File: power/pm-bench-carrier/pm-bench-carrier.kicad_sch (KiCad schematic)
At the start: 47 parts, among them J1 VIN 40-60V, J2 VOUT 19V, Q1 2N7002

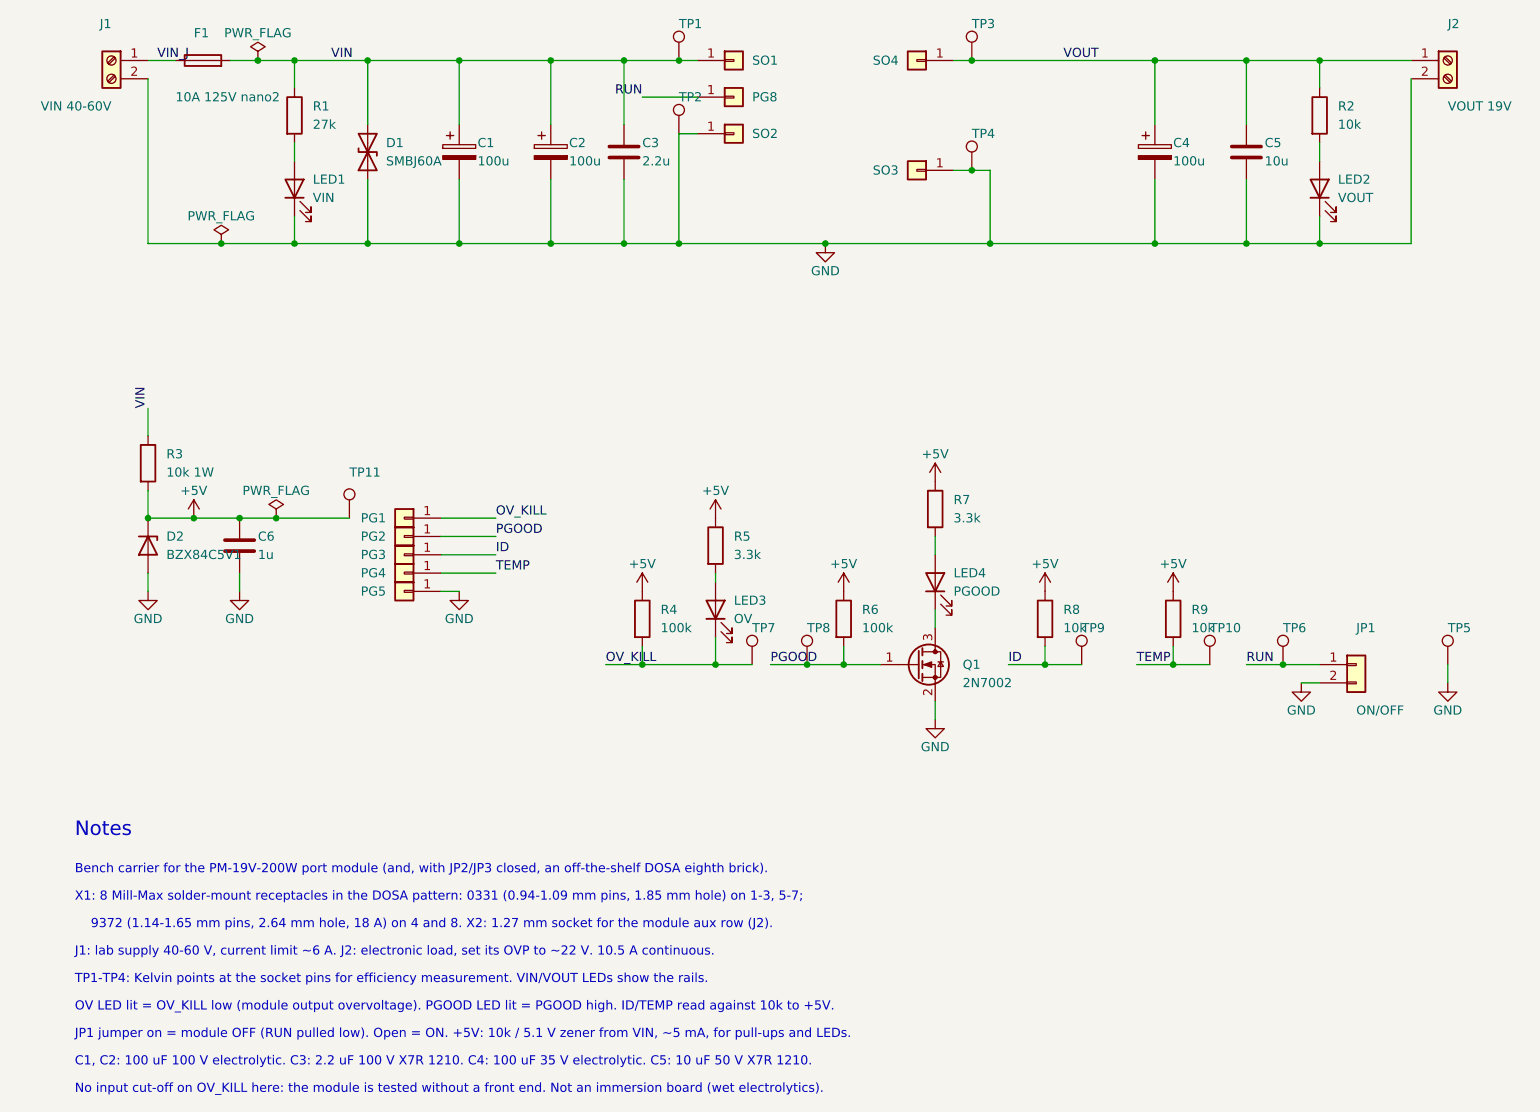
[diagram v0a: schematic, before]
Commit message: Revert "power: screwed PM module mount footprints (M2 into SMT standoffs, pogo aux) on module, plane and bench carrier; RUN moves to aux pad 8; copper not yet rerouted"
This reverts commit abb9f50ba34d0b63e5425fa3cd376420f2890e7d.
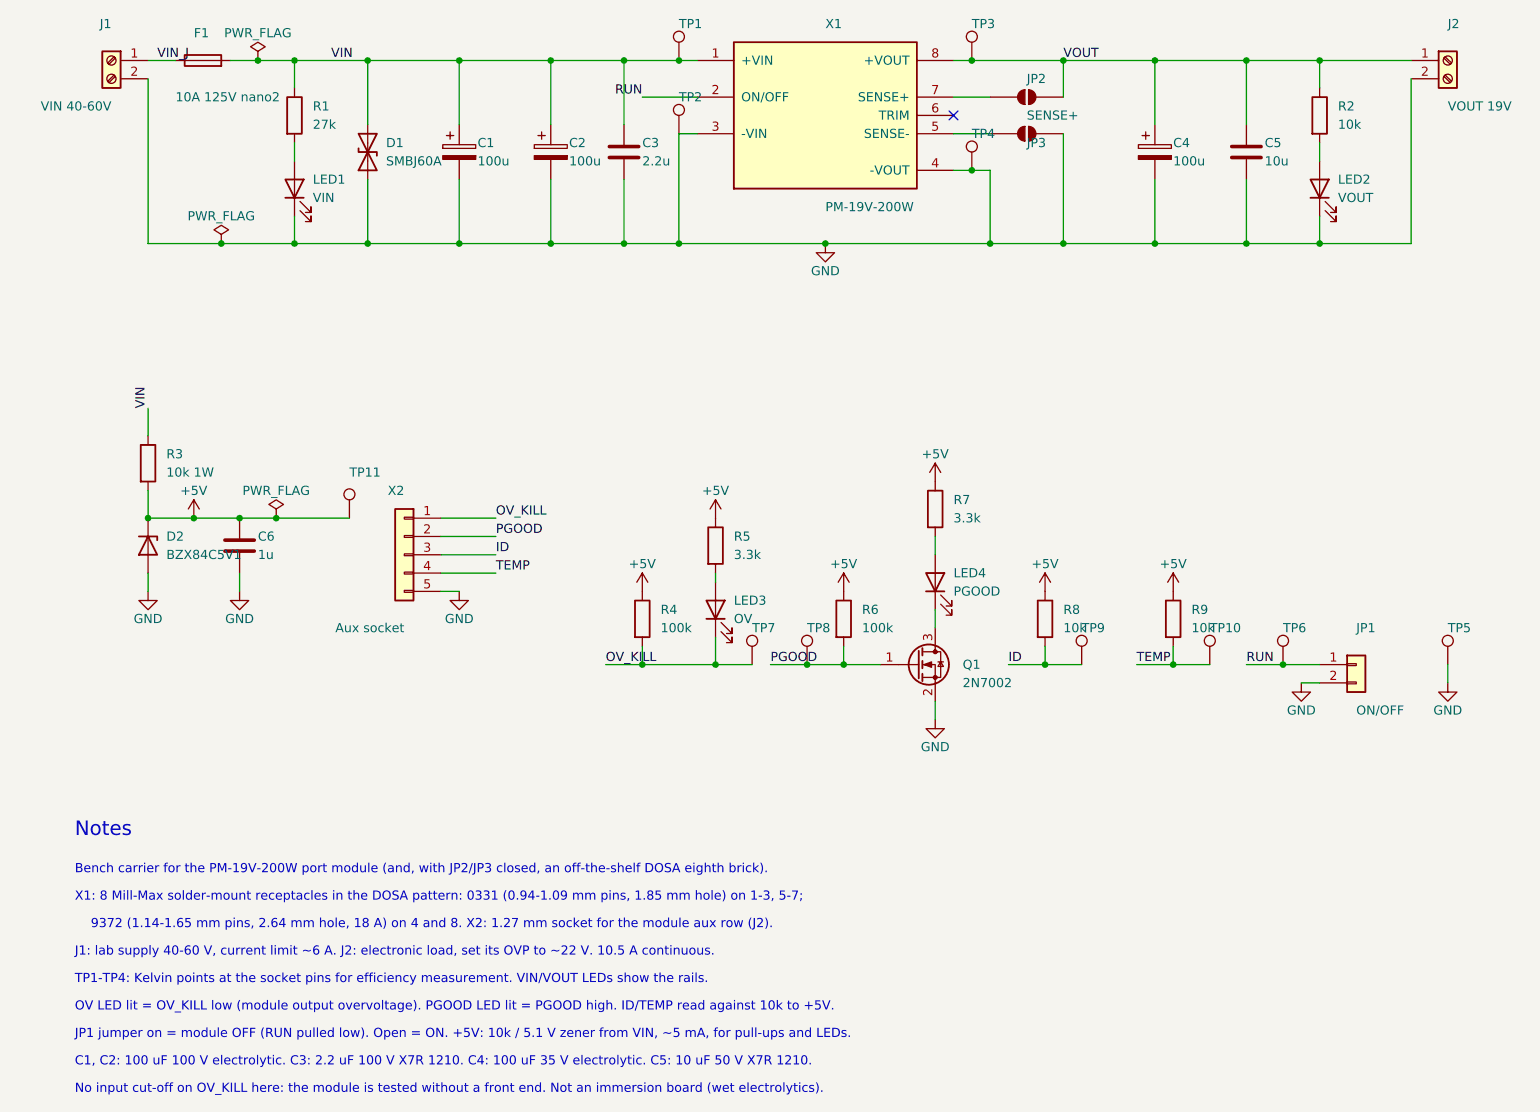
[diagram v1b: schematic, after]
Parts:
- removed PG1, PG2, PG3, PG4, PG5, PG8: pogo, carrier:PM_Pogo_YZ130115073P, symbol Connector_Generic:Conn_01x01
- removed SO1, SO2, SO3, SO4: M2x6 standoff, carrier:PM_Standoff_M2x6_SMTSO, symbol Connector_Generic:Conn_01x01
- added JP2: SENSE+, Jumper:SolderJumper-2_P1.3mm_Open_RoundedPad1.0x1.5mm, symbol Jumper:SolderJumper_2_Open
- added JP3: SENSE-, Jumper:SolderJumper-2_P1.3mm_Open_RoundedPad1.0x1.5mm, symbol Jumper:SolderJumper_2_Open
- added X1: PM-19V-200W, carrier:Brick_Eighth_DOSA_Socket, symbol carrier:PM_Brick_Socket
- added X2: Aux socket, Connector_PinSocket_1.27mm:PinSocket_1x05_P1.27mm_Vertical, symbol Connector_Generic:Conn_01x05
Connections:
- net GND: now also JP3.2 (B), X1.3 (-VIN), X1.4 (-VOUT), X2.5 (Pin_5)
- net ID: now also X2.3 (Pin_3)
- net OV_KILL: now also X2.1 (Pin_1)
- net PGOOD: now also X2.2 (Pin_2)
- net RUN: now also X1.2 (ON/OFF)
- net TEMP: now also X2.4 (Pin_4)
- net VIN: now also X1.1 (+VIN)
- net VOUT: now also JP2.2 (B), X1.8 (+VOUT)
- new net: JP2.1 (A), X1.7 (SENSE+)
- new net: JP3.1 (A), X1.5 (SENSE-)
- no-connect marks 0 -> 1

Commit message: power: screwed PM module mount footprints (M2 into SMT standoffs, pogo aux) on module, plane and bench carrier; RUN moves to aux pad 8; copper not yet rerouted
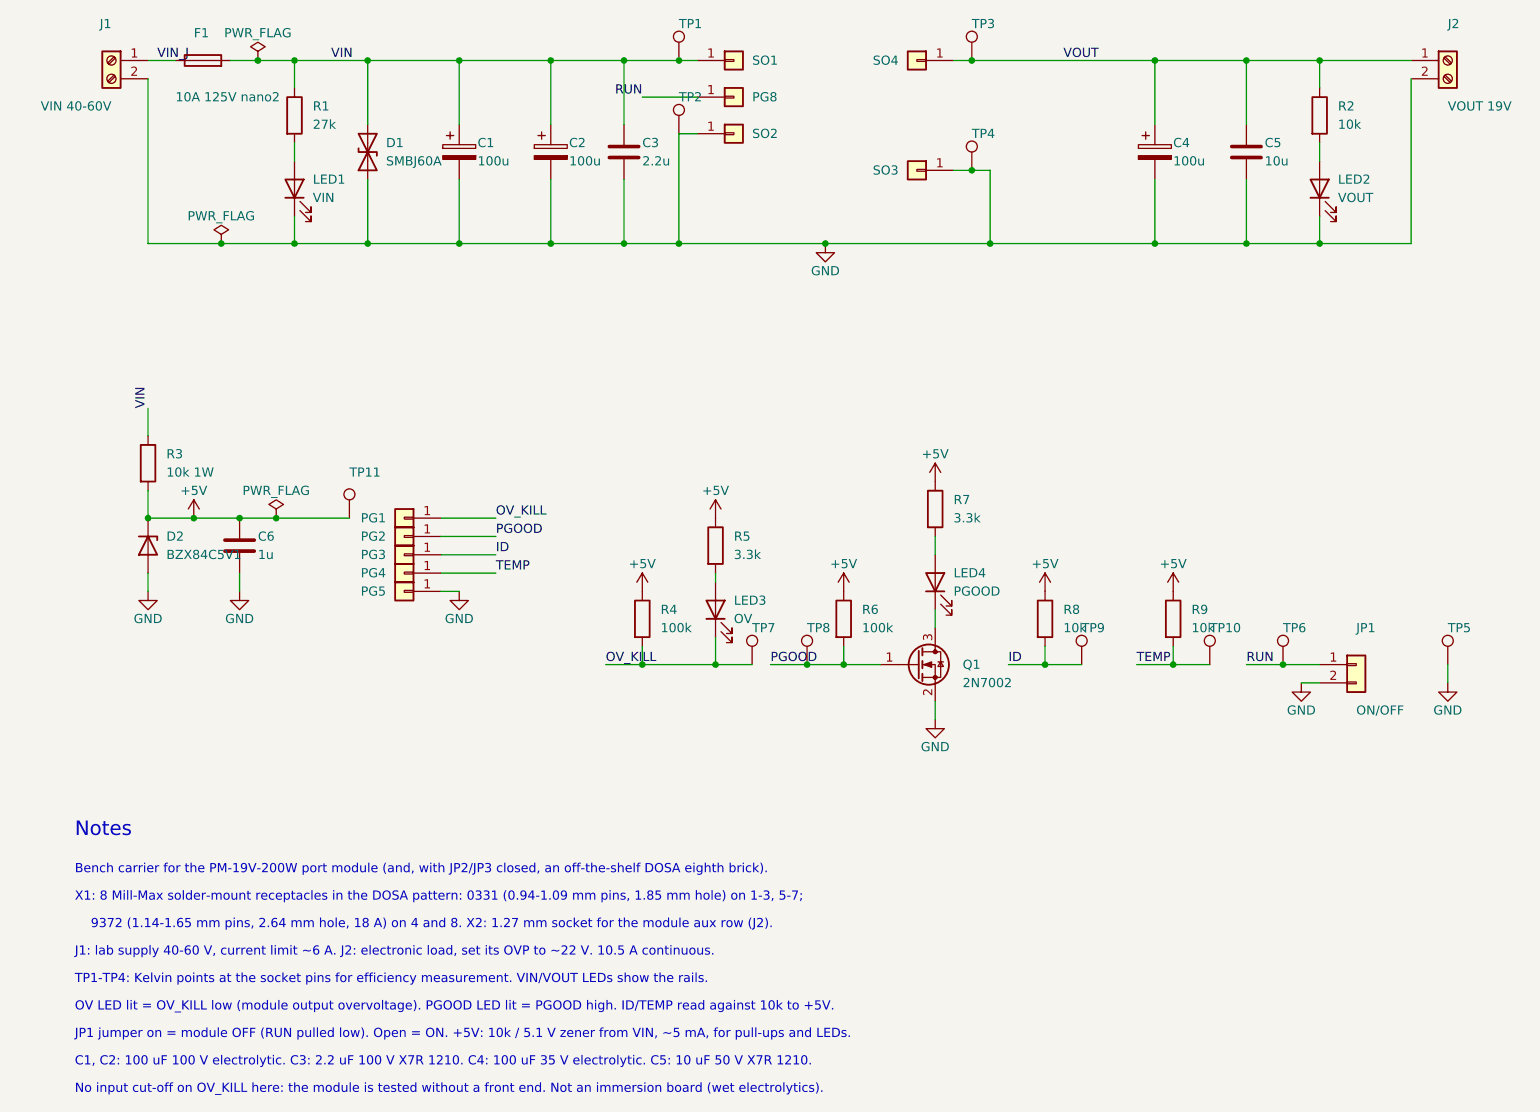
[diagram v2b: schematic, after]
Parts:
- removed JP2: SENSE+, Jumper:SolderJumper-2_P1.3mm_Open_RoundedPad1.0x1.5mm, symbol Jumper:SolderJumper_2_Open
- removed JP3: SENSE-, Jumper:SolderJumper-2_P1.3mm_Open_RoundedPad1.0x1.5mm, symbol Jumper:SolderJumper_2_Open
- removed X1: PM-19V-200W, carrier:Brick_Eighth_DOSA_Socket, symbol carrier:PM_Brick_Socket
- removed X2: Aux socket, Connector_PinSocket_1.27mm:PinSocket_1x05_P1.27mm_Vertical, symbol Connector_Generic:Conn_01x05
- added PG1, PG2, PG3, PG4, PG5, PG8: pogo, carrier:PM_Pogo_YZ130115073P, symbol Connector_Generic:Conn_01x01
- added SO1, SO2, SO3, SO4: M2x6 standoff, carrier:PM_Standoff_M2x6_SMTSO, symbol Connector_Generic:Conn_01x01
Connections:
- net GND: now also PG5.1 (Pin_1), SO2.1 (Pin_1), SO3.1 (Pin_1)
- net ID: now also PG3.1 (Pin_1)
- net OV_KILL: now also PG1.1 (Pin_1)
- net PGOOD: now also PG2.1 (Pin_1)
- net RUN: now also PG8.1 (Pin_1)
- net TEMP: now also PG4.1 (Pin_1)
- net VIN: now also SO1.1 (Pin_1)
- net VOUT: now also SO4.1 (Pin_1)
- no-connect marks 1 -> 0
